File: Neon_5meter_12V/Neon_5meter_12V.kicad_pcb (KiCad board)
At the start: 2 copper layers, 77.5 x 51.5 mm, 47 parts, among them J2 Barrel_Jack_MountingPin, J4 Barrel_Jack_MountingPin, J5 Barrel_Jack_MountingPin, J6 Conn_01x03_Pin, Q1 IRLML2502TRPBF, Q2 IRLML2502TRPBF, Q3 BSS138, Q4 BSS138, Q5 BSS138, SW1 SW_Push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

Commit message: fast routing
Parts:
- moved R6 5.62 mm to (176.4, 41.5)
- moved D11 4.98 mm to (126.1, 37.2), turned to 180 degrees
- moved Q2 3.93 mm to (180.9, 41.5)
- moved R12 1.30 mm to (130.1, 55.1)
- moved R5 1.27 mm to (171.9, 40.9)
- moved R2 1.14 mm to (169.6, 45.4)
- moved R16 0.90 mm to (140.7, 52.0)
- moved D9 0.61 mm to (136.0, 61.3)
- moved R17 0.32 mm to (139.7, 58.6)
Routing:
- net +12V: track 0.00 -> 102.3 mm, vias 0 -> 1
- net +3V3: track 0.00 -> 83.1 mm, vias 0 -> 2
- net ESP_EN: track 0.00 -> 27.5 mm, vias 0 -> 2
- net B_Jack: track 0.00 -> 26.1 mm
- net Net-(D11-RK): track 0.00 -> 23.3 mm
- net Net-(Q1-G): track 0.00 -> 20.1 mm
- net ESP_IO27: track 0.00 -> 18.5 mm, vias 0 -> 2
- net P_Jack: track 0.00 -> 17.1 mm
- net ESP_U0RX: track 0.00 -> 15.4 mm
- net Net-(D11-GK): track 0.00 -> 14.6 mm
- net ESP_U0TX: track 0.00 -> 12.7 mm
- net ESP_IO0: track 0.00 -> 12.5 mm
- net Net-(D1-K): track 0.00 -> 12.0 mm
- net ESP_IO26: track 0.00 -> 10.1 mm
- net Net-(Q5-G): track 0.00 -> 9.20 mm
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
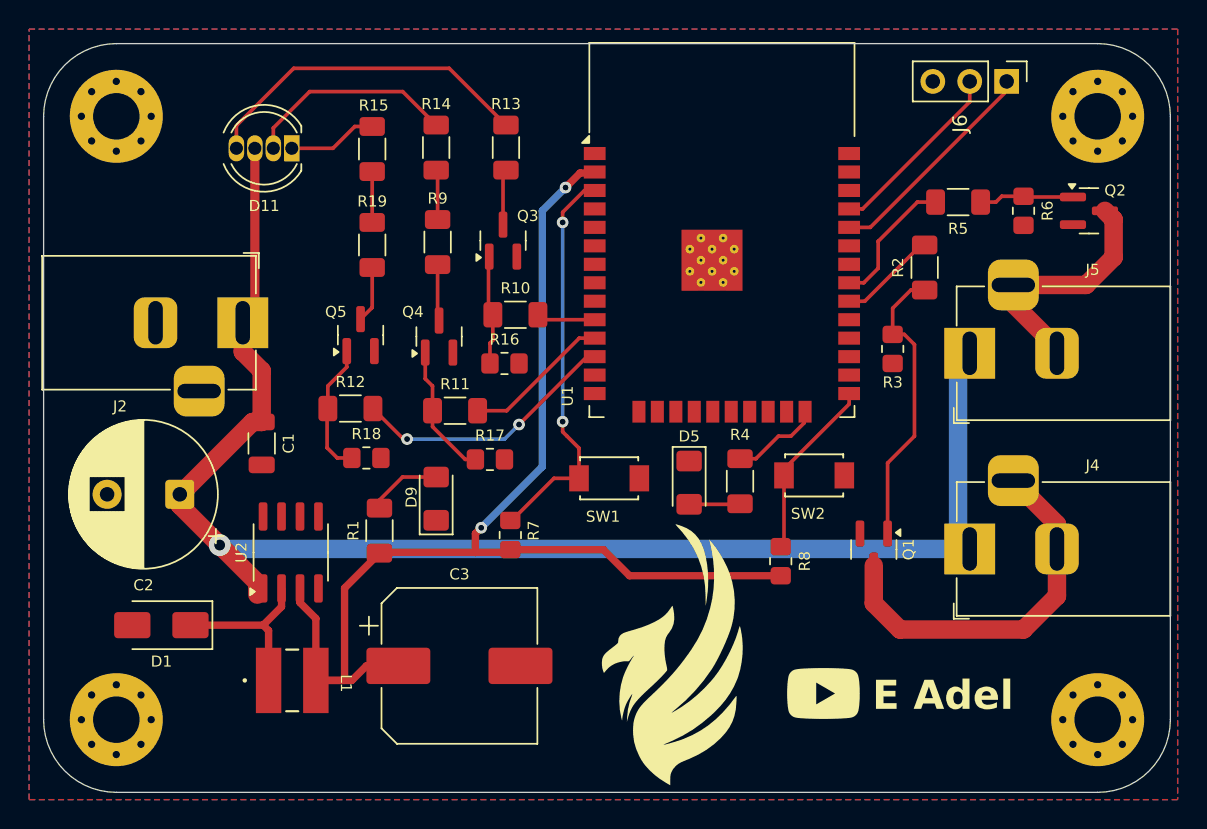
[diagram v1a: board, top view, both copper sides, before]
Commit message: updated tutankhamon logo
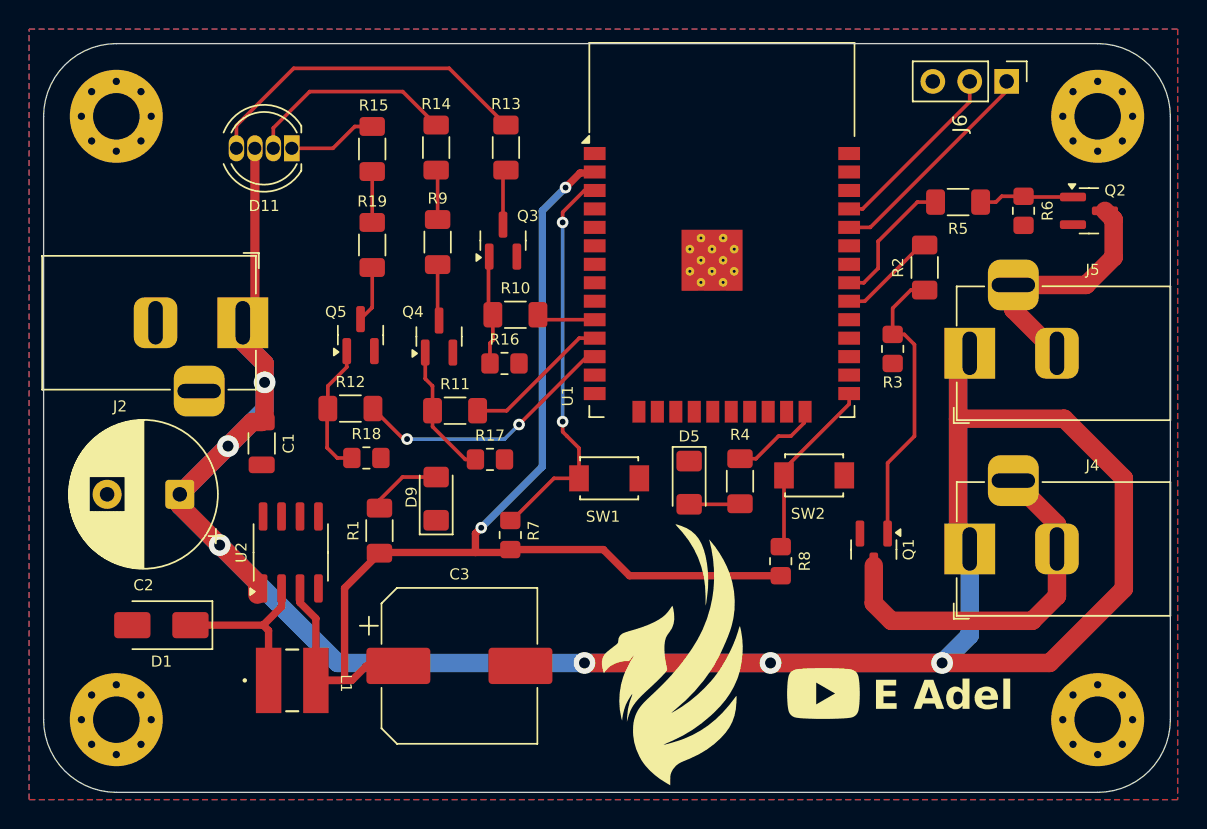
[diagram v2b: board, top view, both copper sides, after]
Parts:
- moved G*** 12.8 mm to (148.6, 48.9), turned to 0 degrees
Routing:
- net +12V: track 102.3 -> 206.0 mm, vias 1 -> 6

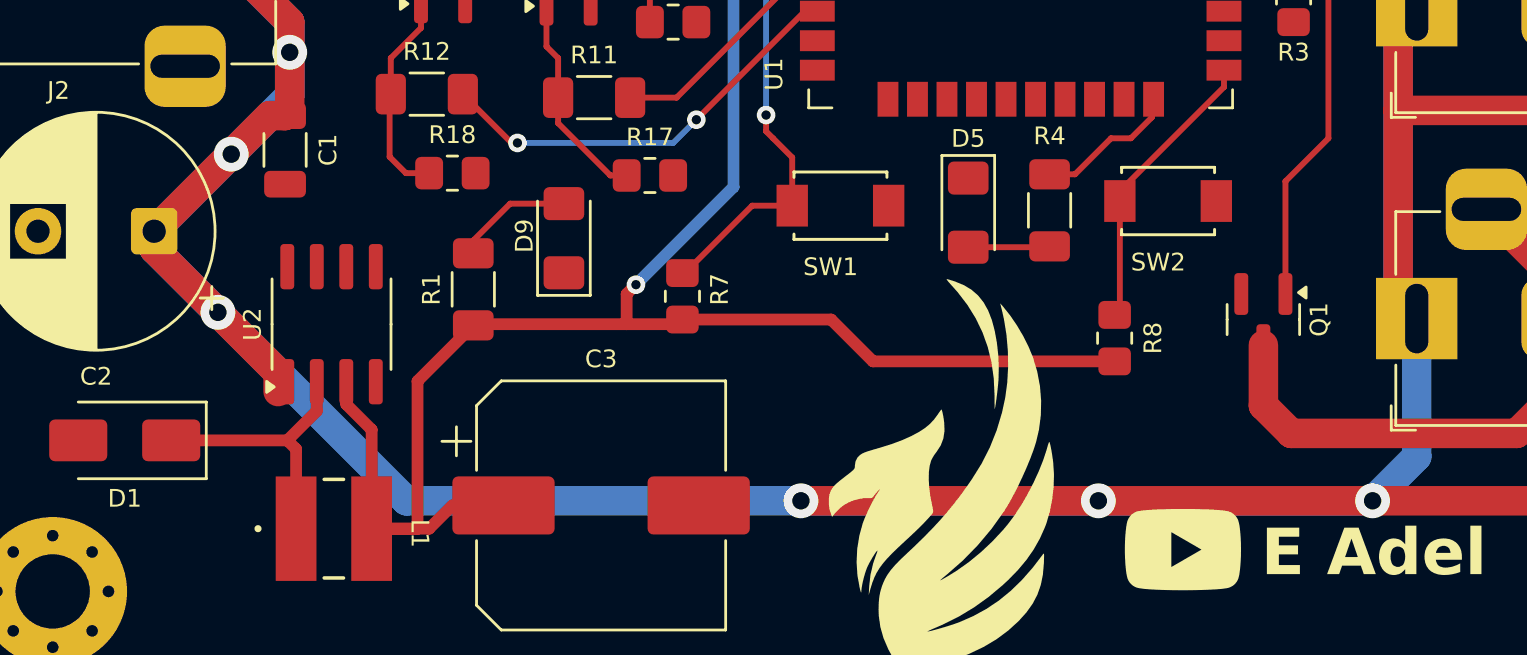
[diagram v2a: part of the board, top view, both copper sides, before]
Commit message: updated routing and tutankhamon place on b.silkscreen
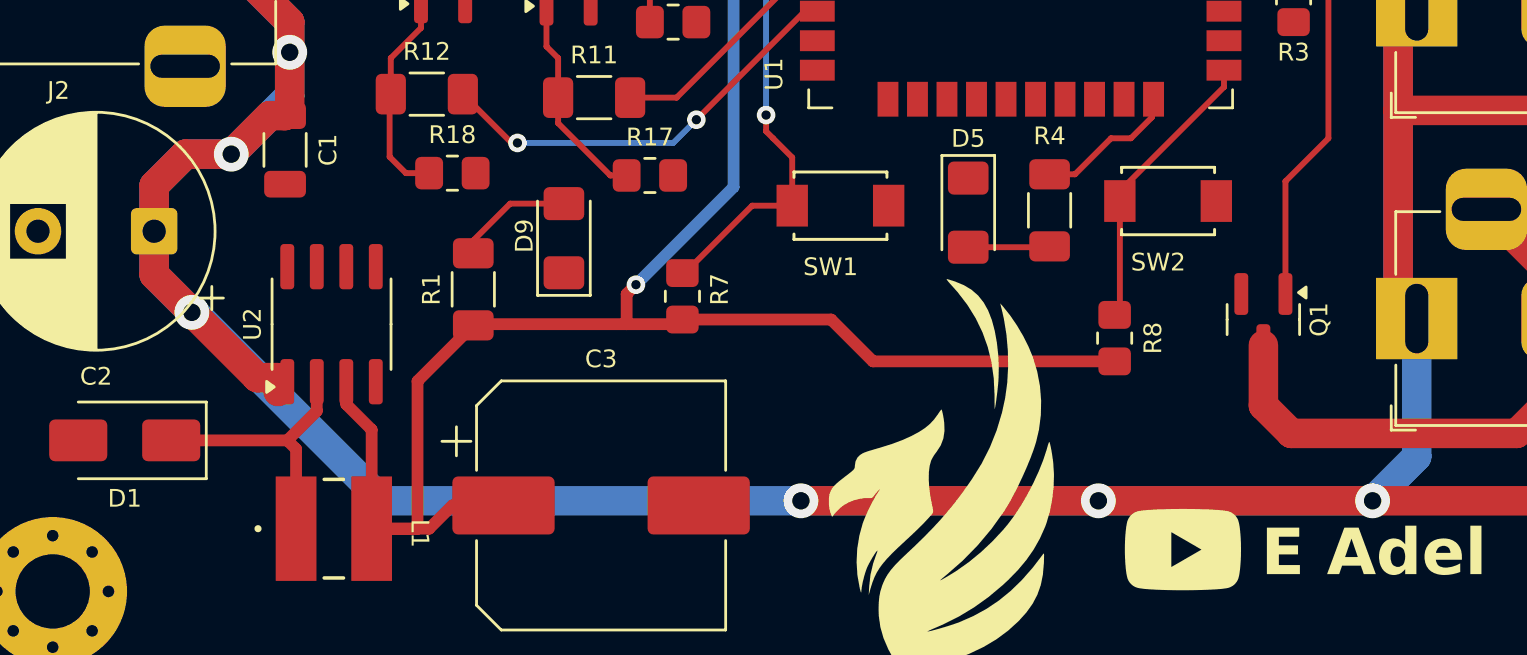
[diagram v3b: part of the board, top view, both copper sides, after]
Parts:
- moved G*** 0.81 mm to (147.8, 48.8)
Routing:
- net +12V: track 206.0 -> 209.5 mm
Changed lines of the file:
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@@
 	(footprint "LOGO"
 		(layer "F.Cu")
-		(at 148.619596 48.912477)
+		(at 147.819596 48.812477)
 		(property "Reference" "G***"
 			(at 0 0 0)
@@
 	)
 	(gr_text "Made on Earth\nby pharaohs"
-		(at 149.2 65.9 180)
+		(at 147.5 67.1 0)
 		(layer "B.SilkS")
 		(effects
@@
 				(thickness 0.225)
 			)
-			(justify bottom mirror)
+			(justify mirror)
 		)
 	)
@@
 	)
 	(segment
-		(start 118.367677 61)
-		(end 121.683838 57.683838)
+		(start 119.99 64.49)
+		(end 122.8 67.3)
 		(width 1.27)
 		(layer "F.Cu")
@@
 	)
 	(segment
-		(start 118.367677 61)
-		(end 118.367677 61.757677)
+		(start 119.716162 57.683838)
+		(end 121.683838 57.683838)
 		(width 1.27)
 		(layer "F.Cu")
@@
 	)
 	(segment
-		(start 121.11 64.49)
-		(end 123.7 67.08)
-		(width 1.27)
-		(layer "F.Cu")
-		(net 1)
-	)
-	(segment
 		(start 123.53 37.2)
 		(end 123.53 48.37)
@@
 	)
 	(segment
-		(start 122.7 49.2)
-		(end 122.7 50.5)
+		(start 118.367677 59.032323)
+		(end 119.716162 57.683838)
+		(width 1.27)
+		(layer "F.Cu")
+		(net 1)
+	)
+	(segment
+		(start 119.99 64.49)
+		(end 118.367677 62.867677)
 		(width 1.27)
 		(layer "F.Cu")
@@
 	)
 	(segment
-		(start 121.1 64.49)
-		(end 121.11 64.49)
+		(start 118.367677 61)
+		(end 118.367677 59.032323)
+		(width 1.27)
+		(layer "F.Cu")
+		(net 1)
+	)
+	(segment
+		(start 123.7 67.3)
+		(end 123.7 67.9)
+		(width 1.27)
+		(layer "F.Cu")
+		(net 1)
+	)
+	(segment
+		(start 122.7 49.2)
+		(end 122.7 50.5)
 		(width 1.27)
 		(layer "F.Cu")
@@
 	)
 	(segment
-		(start 123.7 67.08)
-		(end 123.7 67.9)
+		(start 118.367677 62.867677)
+		(end 118.367677 61)
 		(width 1.27)
 		(layer "F.Cu")
@@
 	)
 	(segment
-		(start 159 72.6)
-		(end 170.8 72.6)
+		(start 122.8 67.3)
+		(end 123.7 67.3)
 		(width 1.27)
 		(layer "F.Cu")
@@
 	)
 	(segment
-		(start 118.367677 61.757677)
-		(end 121.1 64.49)
+		(start 159 72.6)
+		(end 170.8 72.6)
 		(width 1.27)
 		(layer "F.Cu")
@@
 	)
 	(via
-		(at 121.11 64.49)
+		(at 119.99 64.49)
 		(size 1.5)
 		(drill 0.75)
@@
 	)
 	(segment
-		(start 118.367677 61.767677)
-		(end 118.367677 61)
-		(width 1.27)
-		(layer "B.Cu")
-		(net 1)
-	)
-	(segment
-		(start 121.11 64.49)
-		(end 121.09 64.49)
+		(start 118.367677 59.032323)
+		(end 119.716162 57.683838)
 		(width 1.27)
 		(layer "B.Cu")
@@
 	)
 	(segment
+		(start 118.367677 62.867677)
+		(end 118.367677 61)
+		(width 1.27)
+		(layer "B.Cu")
+		(net 1)
+	)
+	(segment
 		(start 170.8 72.6)
 		(end 172.7 70.7)
@@
 	)
 	(segment
-		(start 121.09 64.49)
-		(end 118.367677 61.767677)
+		(start 119.99 64.49)
+		(end 120.09 64.49)
+		(width 1.27)
+		(layer "B.Cu")
+		(net 1)
+	)
+	(segment
+		(start 119.99 64.49)
+		(end 118.367677 62.867677)
+		(width 1.27)
+		(layer "B.Cu")
+		(net 1)
+	)
+	(segment
+		(start 119.716162 57.683838)
+		(end 121.683838 57.683838)
 		(width 1.27)
 		(layer "B.Cu")
@@
 	)
 	(segment
-		(start 121.11 64.49)
-		(end 129.22 72.6)
+		(start 128.2 72.6)
+		(end 170.8 72.6)
 		(width 1.27)
 		(layer "B.Cu")
@@
 	)
 	(segment
-		(start 118.367677 61)
-		(end 121.683838 57.683838)
+		(start 120.09 64.49)
+		(end 128.2 72.6)
 		(width 1.27)
 		(layer "B.Cu")
@@
 	)
 	(segment
-		(start 129.22 72.6)
-		(end 170.8 72.6)
+		(start 118.367677 61)
+		(end 118.367677 59.032323)
 		(width 1.27)
 		(layer "B.Cu")
